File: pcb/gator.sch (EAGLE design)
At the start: 77 parts, among them J2 POWER_JACKPTH, Y1 12MHz

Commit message: Routed power for SDRAM
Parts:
- removed USBA: USB-A-S, SparkFun-Connectors:USB-A-S
- added FPGA_JTAG: 87758-14, con-molex-milli-grid:87758-14
- added X1: USB-A-S, SparkFun-Connectors:USB-A-S
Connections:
- removed net FPGA_CLK2: FPGAB1.IO_L34P_1
- new net FPGA_TCK: FPGABNA.TCK, FPGA_JTAG.6
- new net FPGA_TDI: FPGABNA.TDI, FPGA_JTAG.10
- new net FPGA_TDO: FPGABNA.TDO, FPGA_JTAG.8
- new net FPGA_TMS: FPGABNA.TMS, FPGA_JTAG.4
- net 50MHZ_OSC: now also FPGAB1.IO_L41N_GCLK8_1
- net D2: now also FPGAB1.IO_L34P_1; no longer FPGAB1.IO_L40P_GCLK11_1
- net D3: now also FPGAB1.IO_L34N_1; no longer FPGAB1.IO_L40N_GCLK10_1
- net DDC_CLK: now also U$2.DDC_CLK; no longer FPGAB0.IO_L65P_SCP3_0
- net DDC_DATA: now also U$2.DDC_DATA; no longer FPGAB0.IO_L66N_SCP0_0
- net FPGA_CLK1: now also FPGAB1.IO_L41P_GCLK9_IRDY1_1; no longer FPGAB1.IO_L34N_1
- net GND: now also FPGABNA.SUSPEND, FPGA_JTAG.11, FPGA_JTAG.13, FPGA_JTAG.3, FPGA_JTAG.5, FPGA_JTAG.7, FPGA_JTAG.9, X1.GND; no longer USBA.GND
- net N$19: now also X1.D+; no longer USBA.D+
- net N$20: now also X1.D-; no longer USBA.D-
- net NOE: now also FPGAB1.IO_L40P_GCLK11_1; no longer FPGAB1.IO_L41P_GCLK9_IRDY1_1
- net NWE: now also FPGAB1.IO_L40N_GCLK10_1; no longer FPGAB1.IO_L41N_GCLK8_1
- net USB_VBUS: now also X1.VBUS; no longer USBA.VBUS
- net VCCIO: now also FPGA_JTAG.2
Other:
- moved on the sheet: C2, C3, C4, C5, MIC5219-5.0YM5, R21, R22, R25

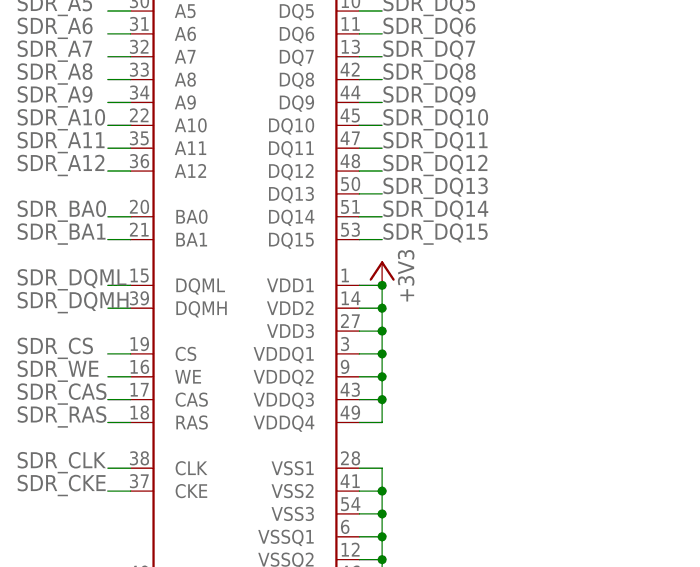
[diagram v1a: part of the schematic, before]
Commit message: Routed some FPGA power and added back ground plane
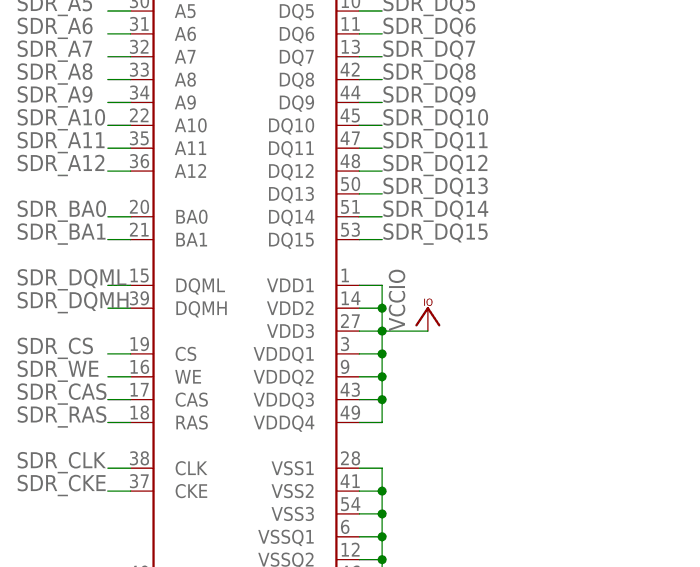
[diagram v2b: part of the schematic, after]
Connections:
- net +3V3: no longer SDRAM.VDD1, SDRAM.VDD2, SDRAM.VDD3, SDRAM.VDDQ1, SDRAM.VDDQ2, SDRAM.VDDQ3, SDRAM.VDDQ4
- net VCCIO: now also SDRAM.VDD1, SDRAM.VDD2, SDRAM.VDD3, SDRAM.VDDQ1, SDRAM.VDDQ2, SDRAM.VDDQ3, SDRAM.VDDQ4
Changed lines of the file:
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@@
 <part name="SUPPLY5" library="supply2" deviceset="GND" device=""/>
 <part name="SUPPLY7" library="supply2" deviceset="GND" device=""/>
-<part name="+3V4" library="supply1" deviceset="+3V3" device=""/>
 <part name="R23" library="SparkFun-Passives" deviceset="RESISTOR" device="0603-RES" value="10K"/>
 <part name="R24" library="SparkFun-Passives" deviceset="RESISTOR" device="0603-RES" value="10K"/>
@@
 <part name="VCC10" library="supply1" deviceset="VCCIO" device=""/>
 <part name="X1" library="SparkFun-Connectors" deviceset="USB" device="-A-S"/>
+<part name="VCC11" library="supply1" deviceset="VCCIO" device=""/>
 </parts>
 <sheets>
@@
 <instance part="SUPPLY5" gate="GND" x="-7.62" y="137.16"/>
 <instance part="SUPPLY7" gate="GND" x="38.1" y="40.64"/>
-<instance part="+3V4" gate="G$1" x="38.1" y="81.28" smashed="yes">
-<attribute name="VALUE" x="41.656" y="76.708" size="1.778" layer="96" rot="R90"/>
-</instance>
 <instance part="R23" gate="G$1" x="-330.2" y="434.34" rot="R90"/>
 <instance part="R24" gate="G$1" x="-210.82" y="144.78"/>
@@
 <instance part="VCC10" gate="G$1" x="-414.02" y="284.48"/>
 <instance part="X1" gate="G$1" x="66.04" y="393.7"/>
+<instance part="VCC11" gate="G$1" x="43.18" y="76.2"/>
 </instances>
 <busses>
@@
 </segment>
 <segment>
-<pinref part="SDRAM" gate="G$1" pin="VDD1"/>
-<pinref part="+3V4" gate="G$1" pin="+3V3"/>
-<wire x1="35.56" y1="78.74" x2="38.1" y2="78.74" width="0.1524" layer="91"/>
-<pinref part="SDRAM" gate="G$1" pin="VDD2"/>
-<wire x1="35.56" y1="76.2" x2="38.1" y2="76.2" width="0.1524" layer="91"/>
-<wire x1="38.1" y1="76.2" x2="38.1" y2="78.74" width="0.1524" layer="91"/>
-<pinref part="SDRAM" gate="G$1" pin="VDD3"/>
-<wire x1="35.56" y1="73.66" x2="38.1" y2="73.66" width="0.1524" layer="91"/>
-<wire x1="38.1" y1="73.66" x2="38.1" y2="76.2" width="0.1524" layer="91"/>
-<pinref part="SDRAM" gate="G$1" pin="VDDQ1"/>
-<wire x1="35.56" y1="71.12" x2="38.1" y2="71.12" width="0.1524" layer="91"/>
-<wire x1="38.1" y1="71.12" x2="38.1" y2="73.66" width="0.1524" layer="91"/>
-<pinref part="SDRAM" gate="G$1" pin="VDDQ2"/>
-<wire x1="35.56" y1="68.58" x2="38.1" y2="68.58" width="0.1524" layer="91"/>
-<wire x1="38.1" y1="68.58" x2="38.1" y2="71.12" width="0.1524" layer="91"/>
-<pinref part="SDRAM" gate="G$1" pin="VDDQ3"/>
-<wire x1="35.56" y1="66.04" x2="38.1" y2="66.04" width="0.1524" layer="91"/>
-<wire x1="38.1" y1="66.04" x2="38.1" y2="68.58" width="0.1524" layer="91"/>
-<pinref part="SDRAM" gate="G$1" pin="VDDQ4"/>
-<wire x1="35.56" y1="63.5" x2="38.1" y2="63.5" width="0.1524" layer="91"/>
-<wire x1="38.1" y1="63.5" x2="38.1" y2="66.04" width="0.1524" layer="91"/>
-<junction x="38.1" y="66.04"/>
-<junction x="38.1" y="68.58"/>
-<junction x="38.1" y="71.12"/>
-<junction x="38.1" y="73.66"/>
-<junction x="38.1" y="76.2"/>
-<junction x="38.1" y="78.74"/>
-</segment>
-<segment>
 <pinref part="R24" gate="G$1" pin="2"/>
 <pinref part="+3V5" gate="G$1" pin="+3V3"/>
@@
 <wire x1="-414.02" y1="279.4" x2="-414.02" y2="281.94" width="0.1524" layer="91"/>
 </segment>
-</net>
+<segment>
+<pinref part="SDRAM" gate="G$1" pin="VDD1"/>
+<wire x1="35.56" y1="78.74" x2="38.1" y2="78.74" width="0.1524" layer="91"/>
+<pinref part="SDRAM" gate="G$1" pin="VDD2"/>
+<wire x1="35.56" y1="76.2" x2="38.1" y2="76.2" width="0.1524" layer="91"/>
+<wire x1="38.1" y1="76.2" x2="38.1" y2="78.74" width="0.1524" layer="91"/>
+<pinref part="SDRAM" gate="G$1" pin="VDD3"/>
+<wire x1="35.56" y1="73.66" x2="38.1" y2="73.66" width="0.1524" layer="91"/>
+<wire x1="38.1" y1="73.66" x2="38.1" y2="76.2" width="0.1524" layer="91"/>
+<pinref part="SDRAM" gate="G$1" pin="VDDQ1"/>
+<wire x1="35.56" y1="71.12" x2="38.1" y2="71.12" width="0.1524" layer="91"/>
+<wire x1="38.1" y1="71.12" x2="38.1" y2="73.66" width="0.1524" layer="91"/>
+<pinref part="SDRAM" gate="G$1" pin="VDDQ2"/>
+<wire x1="35.56" y1="68.58" x2="38.1" y2="68.58" width="0.1524" layer="91"/>
+<wire x1="38.1" y1="68.58" x2="38.1" y2="71.12" width="0.1524" layer="91"/>
+<pinref part="SDRAM" gate="G$1" pin="VDDQ3"/>
+<wire x1="35.56" y1="66.04" x2="38.1" y2="66.04" width="0.1524" layer="91"/>
+<wire x1="38.1" y1="66.04" x2="38.1" y2="68.58" width="0.1524" layer="91"/>
+<pinref part="SDRAM" gate="G$1" pin="VDDQ4"/>
+<wire x1="35.56" y1="63.5" x2="38.1" y2="63.5" width="0.1524" layer="91"/>
+<wire x1="38.1" y1="63.5" x2="38.1" y2="66.04" width="0.1524" layer="91"/>
+<junction x="38.1" y="66.04"/>
+<junction x="38.1" y="68.58"/>
+<junction x="38.1" y="71.12"/>
+<junction x="38.1" y="73.66"/>
+<junction x="38.1" y="76.2"/>
+<pinref part="VCC11" gate="G$1" pin="VCCIO"/>
+<wire x1="38.1" y1="73.66" x2="43.18" y2="73.66" width="0.1524" layer="91"/>
+</segment>
+</net>

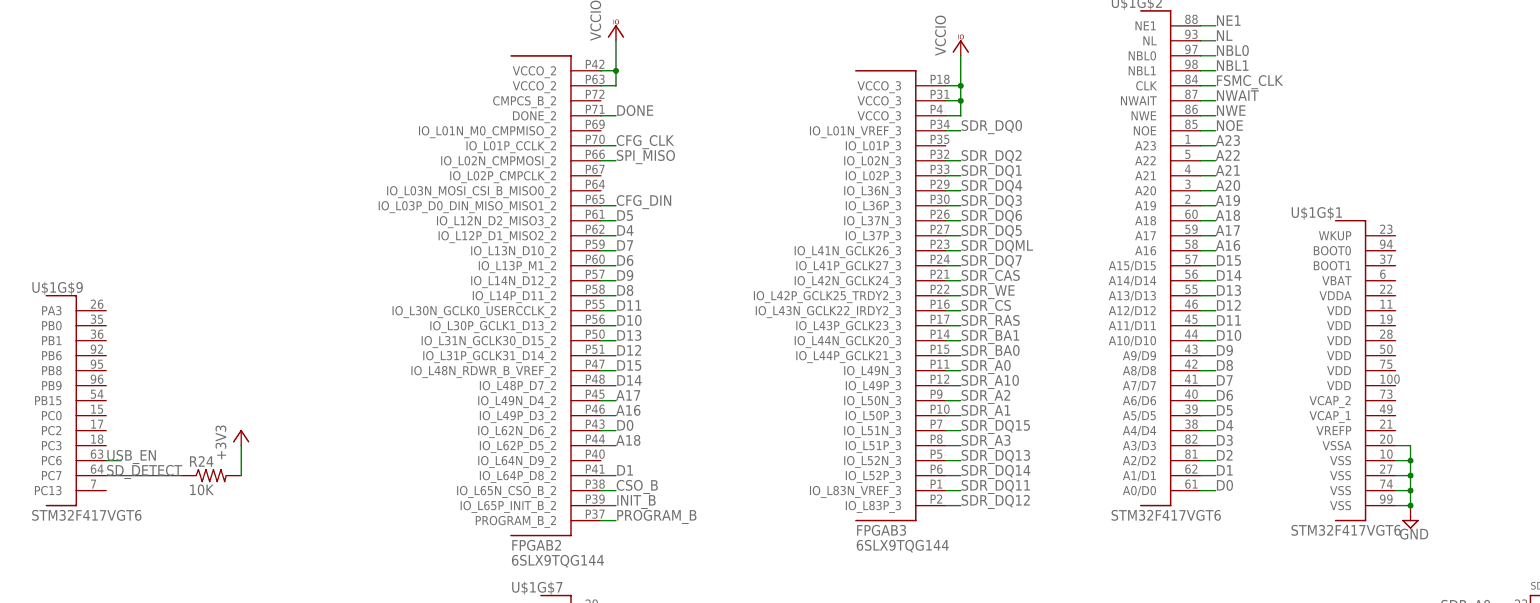
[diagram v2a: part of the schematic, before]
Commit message: Added INIT_B and PROGRAM_B signals needed for slave serial configuration
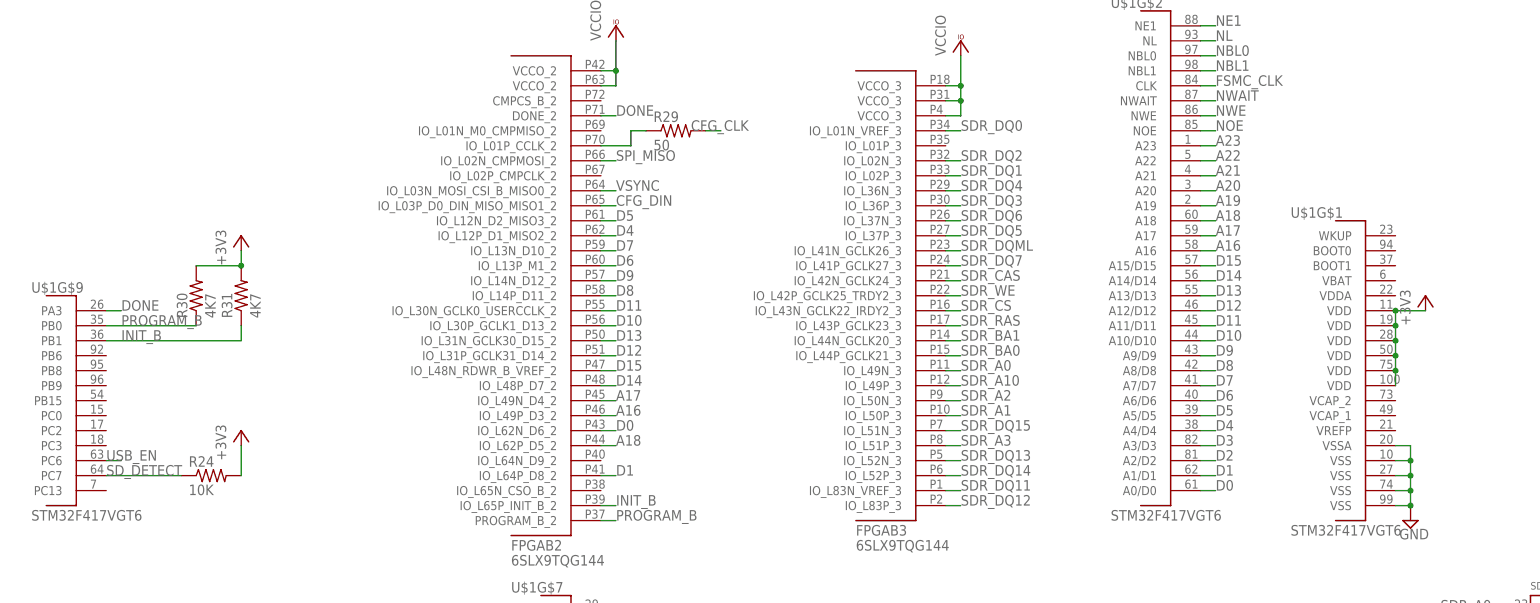
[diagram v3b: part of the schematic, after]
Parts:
- added R29: 50, SparkFun-Passives:RESISTOR0603-RES
- added R30, R31: 4K7, SparkFun-Passives:RESISTOR0603-RES
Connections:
- removed net CSO_B: FPGAB2.IO_L65N_CSO_B_2
- new net N$33: FPGAB2.IO_L01P_CCLK_2, R29.1
- new net VSYNC: FPGAB2.IO_L03N_MOSI_CSI_B_MISO0_2
- net +3V3: now also R30.2, R31.2, U$1G$1.VDD@100, U$1G$1.VDD@11, U$1G$1.VDD@19, U$1G$1.VDD@28, U$1G$1.VDD@50, U$1G$1.VDD@75
- net CFG_CLK: now also R29.2; no longer FPGAB2.IO_L01P_CCLK_2
- net DONE: now also U$1G$9.PA3
- net INIT_B: now also R31.1, U$1G$9.PB1
- net PROGRAM_B: now also R30.1, U$1G$9.PB0
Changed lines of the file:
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@@
 <part name="X1" library="SparkFun-Connectors" deviceset="USB" device="-A-S"/>
 <part name="VCC11" library="supply1" deviceset="VCCIO" device=""/>
+<part name="R29" library="SparkFun-Passives" deviceset="RESISTOR" device="0603-RES" value="50"/>
+<part name="R30" library="SparkFun-Passives" deviceset="RESISTOR" device="0603-RES" value="4K7"/>
+<part name="R31" library="SparkFun-Passives" deviceset="RESISTOR" device="0603-RES" value="4K7"/>
+<part name="+3V4" library="supply1" deviceset="+3V3" device=""/>
+<part name="+3V16" library="supply1" deviceset="+3V3" device=""/>
 </parts>
 <sheets>
@@
 <instance part="X1" gate="G$1" x="66.04" y="393.7"/>
 <instance part="VCC11" gate="G$1" x="43.18" y="76.2"/>
+<instance part="R29" gate="G$1" x="-132.08" y="203.2"/>
+<instance part="R30" gate="G$1" x="-213.36" y="175.26" rot="R90"/>
+<instance part="R31" gate="G$1" x="-205.74" y="175.26" rot="R90"/>
+<instance part="+3V4" gate="G$1" x="-205.74" y="185.42"/>
+<instance part="+3V16" gate="G$1" x="-5.08" y="175.26"/>
 </instances>
 <busses>
@@
 <junction x="-205.74" y="350.52"/>
 </segment>
+<segment>
+<pinref part="R30" gate="G$1" pin="2"/>
+<pinref part="R31" gate="G$1" pin="2"/>
+<wire x1="-213.36" y1="180.34" x2="-205.74" y2="180.34" width="0.1524" layer="91"/>
+<pinref part="+3V4" gate="G$1" pin="+3V3"/>
+<wire x1="-205.74" y1="180.34" x2="-205.74" y2="182.88" width="0.1524" layer="91"/>
+<junction x="-205.74" y="180.34"/>
+</segment>
+<segment>
+<pinref part="U$1" gate="G$1" pin="VDD@100"/>
+<pinref part="U$1" gate="G$1" pin="VDD@11"/>
+<wire x1="-10.16" y1="160.02" x2="-10.16" y2="162.56" width="0.1524" layer="91"/>
+<pinref part="+3V16" gate="G$1" pin="+3V3"/>
+<wire x1="-10.16" y1="162.56" x2="-10.16" y2="165.1" width="0.1524" layer="91"/>
+<wire x1="-10.16" y1="165.1" x2="-10.16" y2="167.64" width="0.1524" layer="91"/>
+<wire x1="-10.16" y1="167.64" x2="-10.16" y2="170.18" width="0.1524" layer="91"/>
+<wire x1="-10.16" y1="170.18" x2="-10.16" y2="172.72" width="0.1524" layer="91"/>
+<wire x1="-10.16" y1="172.72" x2="-5.08" y2="172.72" width="0.1524" layer="91"/>
+<pinref part="U$1" gate="G$1" pin="VDD@19"/>
+<junction x="-10.16" y="170.18"/>
+<pinref part="U$1" gate="G$1" pin="VDD@28"/>
+<junction x="-10.16" y="167.64"/>
+<pinref part="U$1" gate="G$1" pin="VDD@50"/>
+<junction x="-10.16" y="165.1"/>
+<pinref part="U$1" gate="G$1" pin="VDD@75"/>
+<junction x="-10.16" y="162.56"/>
+<junction x="-10.16" y="172.72"/>
+</segment>
 </net>
 <net name="SD_D0" class="0">
@@
 <label x="-142.24" y="205.74" size="1.778" layer="95"/>
 </segment>
+<segment>
+<pinref part="U$1" gate="G$9" pin="PA3"/>
+<wire x1="-228.6" y1="172.72" x2="-226.06" y2="172.72" width="0.1524" layer="91"/>
+<label x="-226.06" y="172.72" size="1.778" layer="95"/>
+</segment>
 </net>
 <net name="INIT_B" class="0">
@@
 <label x="-142.24" y="139.7" size="1.778" layer="95"/>
 </segment>
+<segment>
+<pinref part="U$1" gate="G$9" pin="PB1"/>
+<label x="-226.06" y="167.64" size="1.778" layer="95"/>
+<pinref part="R31" gate="G$1" pin="1"/>
+<wire x1="-228.6" y1="167.64" x2="-205.74" y2="167.64" width="0.1524" layer="91"/>
+<wire x1="-205.74" y1="167.64" x2="-205.74" y2="170.18" width="0.1524" layer="91"/>
+</segment>
 </net>
 <net name="PROGRAM_B" class="0">
@@
 <label x="-142.24" y="137.16" size="1.778" layer="95"/>
 </segment>
-</net>
-<net name="CSO_B" class="0">
-<segment>
-<pinref part="FPGA" gate="B2" pin="IO_L65N_CSO_B_2"/>
-<wire x1="-144.78" y1="142.24" x2="-142.24" y2="142.24" width="0.1524" layer="91"/>
-<label x="-142.24" y="142.24" size="1.778" layer="95"/>
+<segment>
+<pinref part="U$1" gate="G$9" pin="PB0"/>
+<label x="-226.06" y="170.18" size="1.778" layer="95"/>
+<pinref part="R30" gate="G$1" pin="1"/>
+<wire x1="-228.6" y1="170.18" x2="-213.36" y2="170.18" width="0.1524" layer="91"/>
 </segment>
 </net>
@@
 <net name="CFG_CLK" class="0">
 <segment>
-<pinref part="FPGA" gate="B2" pin="IO_L01P_CCLK_2"/>
-<wire x1="-144.78" y1="200.66" x2="-142.24" y2="200.66" width="0.1524" layer="91"/>
-<label x="-142.24" y="200.66" size="1.778" layer="95"/>
-</segment>
-<segment>
 <pinref part="U$1" gate="G$7" pin="SPI1_SCK"/>
 <wire x1="-144.78" y1="119.38" x2="-142.24" y2="119.38" width="0.1524" layer="91"/>
 <label x="-142.24" y="119.38" size="1.778" layer="95"/>
+</segment>
+<segment>
+<pinref part="R29" gate="G$1" pin="2"/>
+<wire x1="-127" y1="203.2" x2="-124.46" y2="203.2" width="0.1524" layer="91"/>
+<label x="-129.54" y="203.2" size="1.778" layer="95"/>
 </segment>
 </net>
@@
 </segment>
 </net>
+<net name="VSYNC" class="0">
+<segment>
+<pinref part="FPGA" gate="B2" pin="IO_L03N_MOSI_CSI_B_MISO0_2"/>
+<wire x1="-144.78" y1="193.04" x2="-142.24" y2="193.04" width="0.1524" layer="91"/>
+<label x="-142.24" y="193.04" size="1.778" layer="95"/>
+</segment>
+</net>
+<net name="N$33" class="0">
+<segment>
+<pinref part="FPGA" gate="B2" pin="IO_L01P_CCLK_2"/>
+<wire x1="-144.78" y1="200.66" x2="-139.7" y2="200.66" width="0.1524" layer="91"/>
+<wire x1="-139.7" y1="200.66" x2="-139.7" y2="203.2" width="0.1524" layer="91"/>
+<pinref part="R29" gate="G$1" pin="1"/>
+<wire x1="-139.7" y1="203.2" x2="-137.16" y2="203.2" width="0.1524" layer="91"/>
+</segment>
+</net>

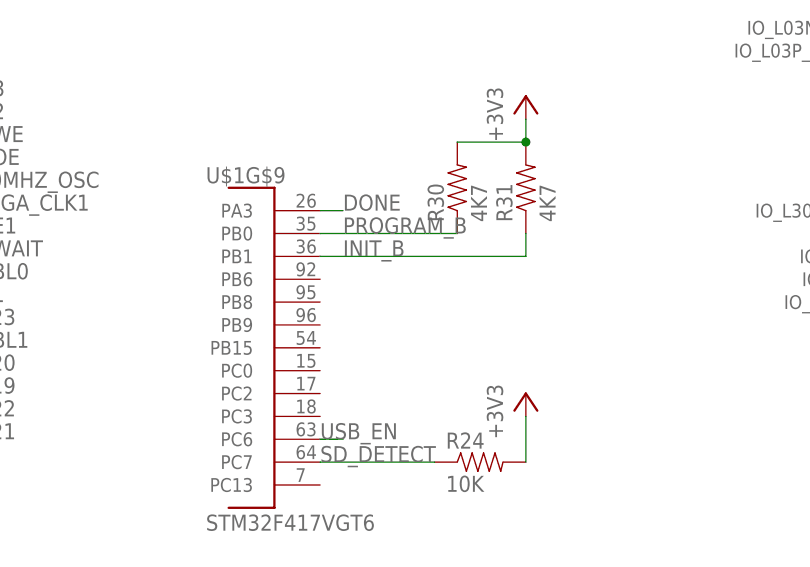
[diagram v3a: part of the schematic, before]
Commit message: Routed power to ARM, added VSync signal
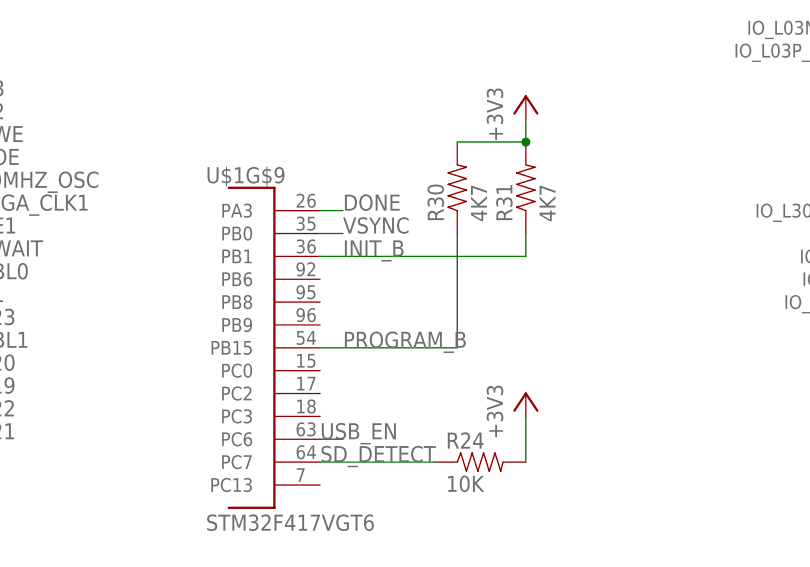
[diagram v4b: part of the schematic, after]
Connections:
- net PROGRAM_B: now also U$1G$9.PB15; no longer U$1G$9.PB0
- net VSYNC: now also U$1G$9.PB0
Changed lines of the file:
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@@
 </segment>
 <segment>
-<pinref part="U$1" gate="G$9" pin="PB0"/>
-<label x="-226.06" y="170.18" size="1.778" layer="95"/>
+<pinref part="U$1" gate="G$9" pin="PB15"/>
+<label x="-226.06" y="157.48" size="1.778" layer="95"/>
 <pinref part="R30" gate="G$1" pin="1"/>
-<wire x1="-228.6" y1="170.18" x2="-213.36" y2="170.18" width="0.1524" layer="91"/>
+<wire x1="-228.6" y1="157.48" x2="-213.36" y2="157.48" width="0.1524" layer="91"/>
+<wire x1="-213.36" y1="157.48" x2="-213.36" y2="170.18" width="0.1524" layer="91"/>
 </segment>
 </net>
@@
 <label x="-142.24" y="193.04" size="1.778" layer="95"/>
 </segment>
-</net>
+<segment>
+<pinref part="U$1" gate="G$9" pin="PB0"/>
+<wire x1="-228.6" y1="170.18" x2="-226.06" y2="170.18" width="0.1524" layer="91"/>
+<label x="-226.06" y="170.18" size="1.778" layer="95"/>
+</segment>
+</net>

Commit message: any recent changes before break
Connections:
- net N$10 renamed RD-
- net N$11 renamed TD+
- net N$12 renamed TD-
- net N$9 renamed RD+
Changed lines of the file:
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@@
 </segment>
 </net>
-<net name="N$9" class="0">
+<net name="RD+" class="0">
 <segment>
 <pinref part="ETH_PHY" gate="G$1" pin="RD+"/>
@@
 </segment>
 </net>
-<net name="N$10" class="0">
+<net name="RD-" class="0">
 <segment>
 <pinref part="ETH_PHY" gate="G$1" pin="RD-"/>
@@
 </segment>
 </net>
-<net name="N$11" class="0">
+<net name="TD+" class="0">
 <segment>
 <pinref part="ETH_PHY" gate="G$1" pin="TD+"/>
@@
 </segment>
 </net>
-<net name="N$12" class="0">
+<net name="TD-" class="0">
 <segment>
 <pinref part="ETH_PHY" gate="G$1" pin="TD-"/>
